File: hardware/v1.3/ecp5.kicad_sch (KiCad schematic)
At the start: 1 part, among them U1 ECP5-CABGA256

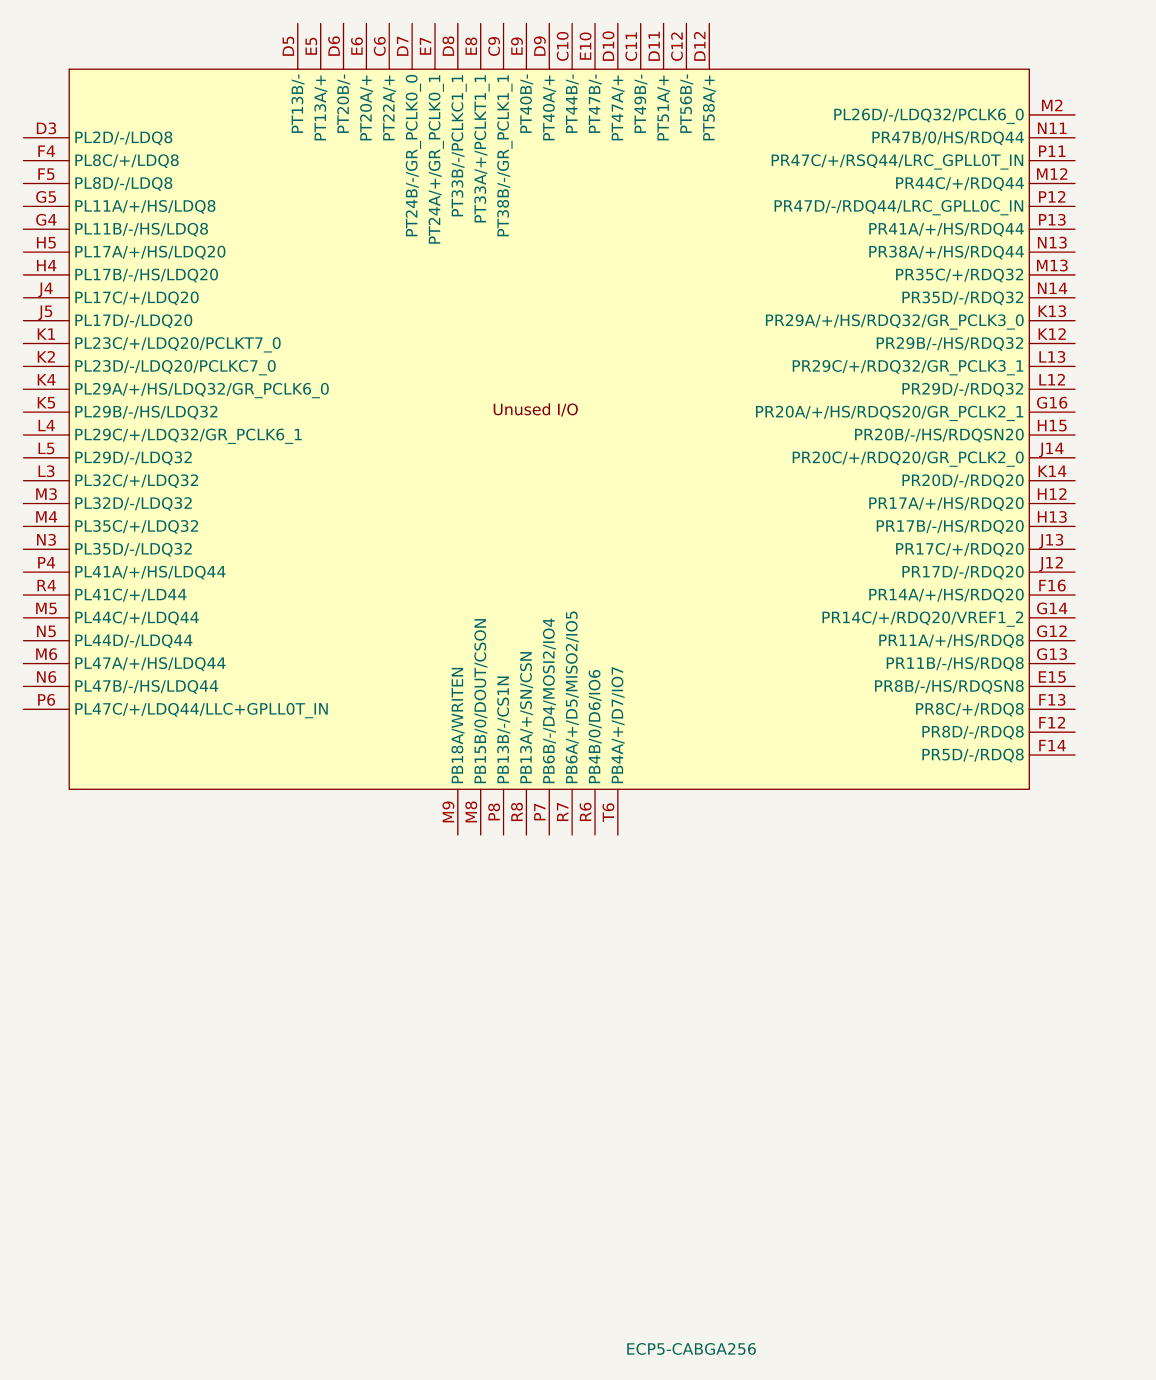
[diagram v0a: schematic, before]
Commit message: Refine README
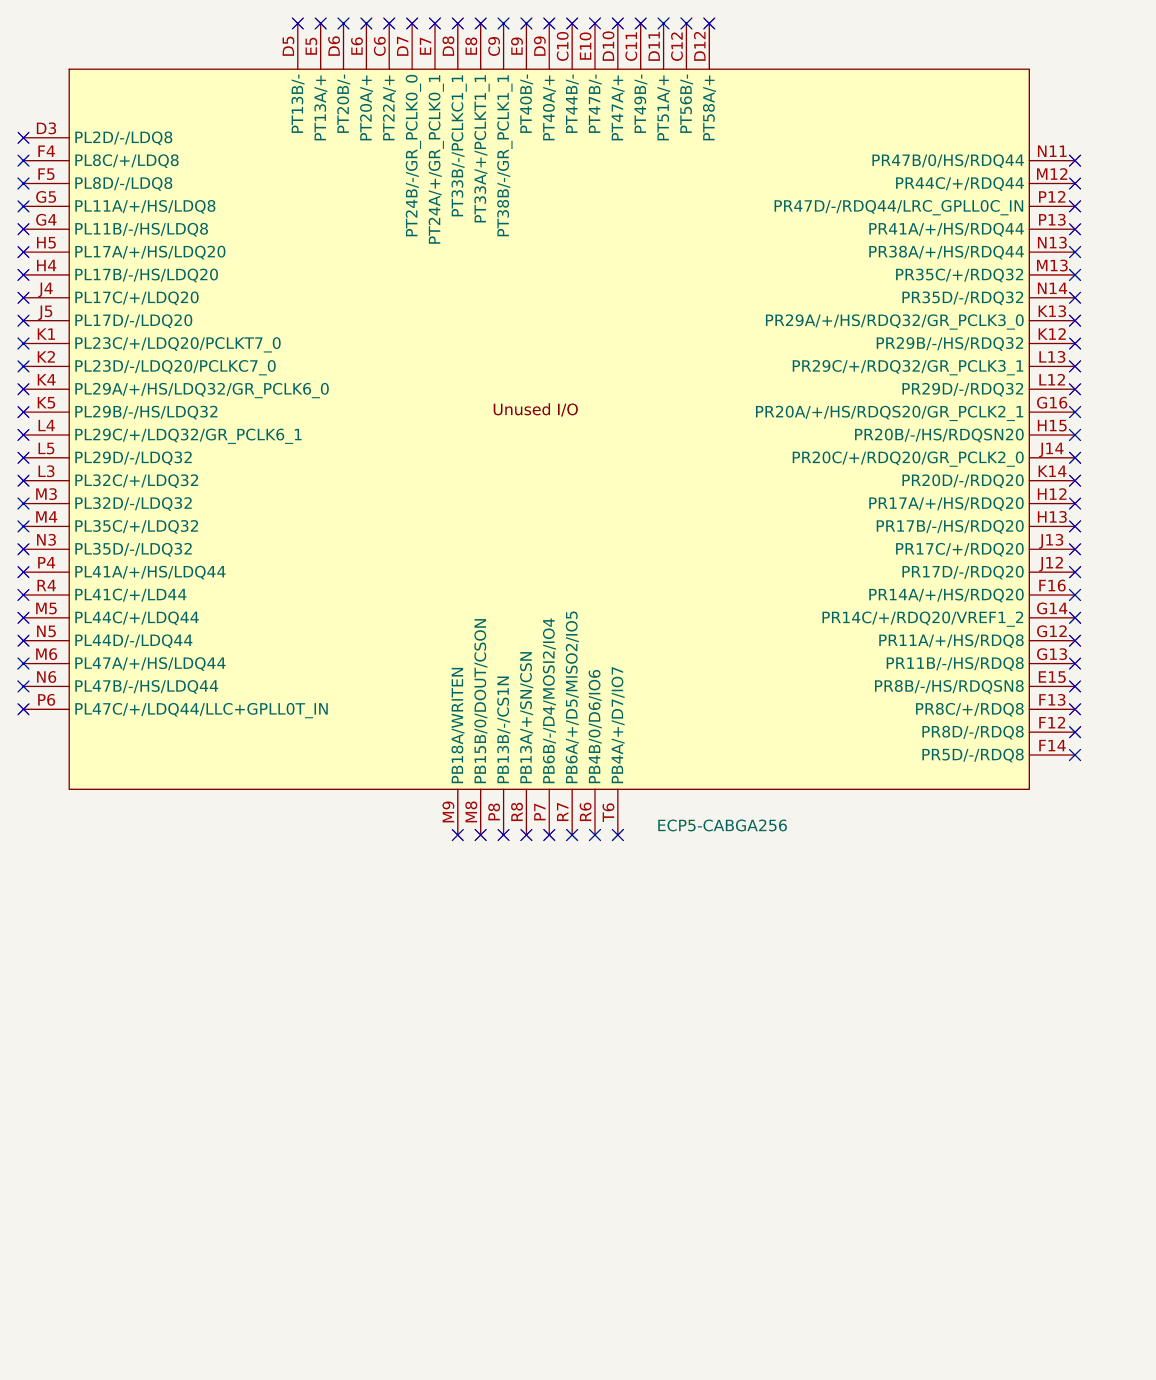
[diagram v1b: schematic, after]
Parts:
- U1: LCSC Link (none) -> https://lcsc.com/product-detail/Programmable-Logic-Device-C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; LCSC Part # (none) -> C1521614; Manufactuer Part Number (none) -> LFE5U-25F-6BG256C
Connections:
- no-connect marks 0 -> 80
